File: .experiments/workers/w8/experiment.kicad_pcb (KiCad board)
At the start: 2 copper layers, 140 x 90 mm, 39 parts, among them J1 USB_C, J2 Output, J3 Debug, Q1 FS8205A, U1 USBLC6-2SC6, U2 BQ24072, U3 HY2113-KB5B, U4 MT3608, U5 AP2112K-3.3, U6 LN61CN3302MR-G

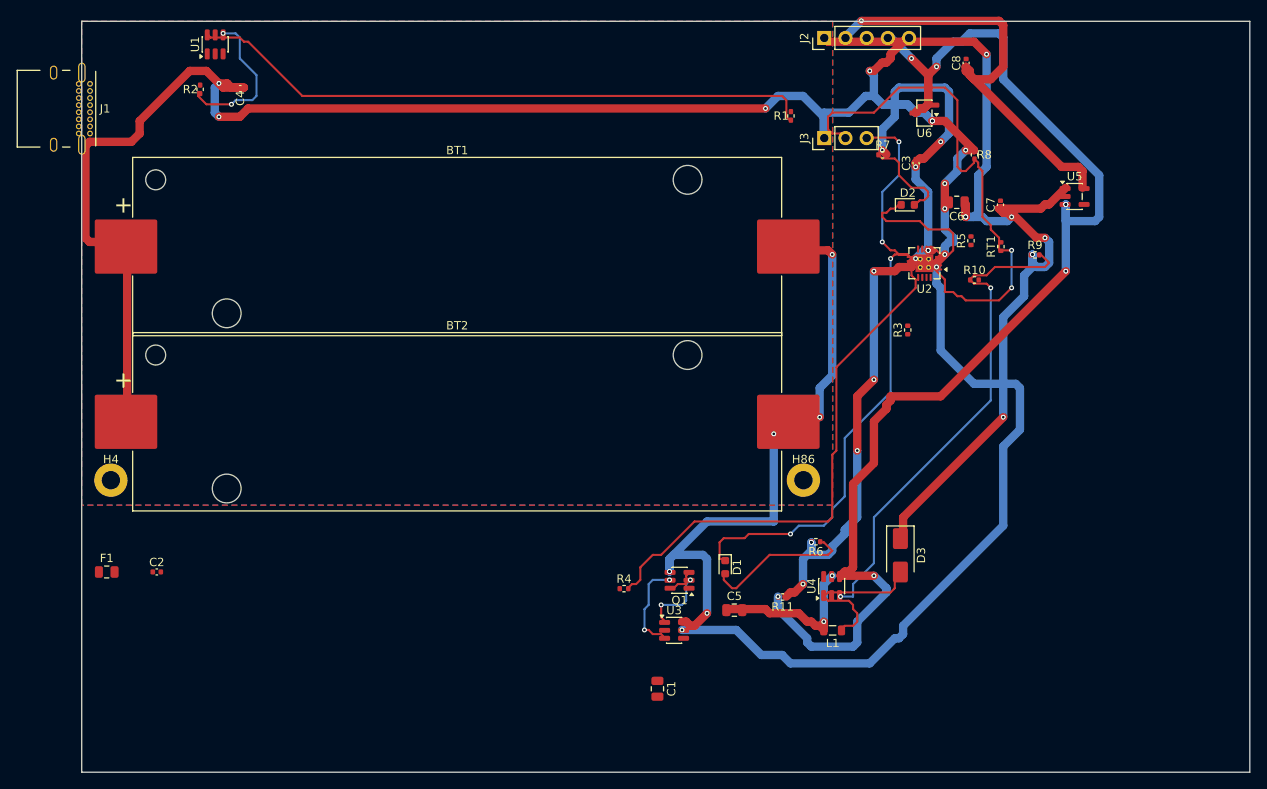
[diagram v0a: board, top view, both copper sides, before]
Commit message: 35-round experiment: best score 25.33, improved routing params
Router and conflict resolution tuning from autonomous optimization loop.
Best config: clearance=0.2051mm, cooling_factor=0.9735, existing_trace_cost=200.0

Co-Authored-By: Claude Opus 4.6 <noreply@anthropic.com>
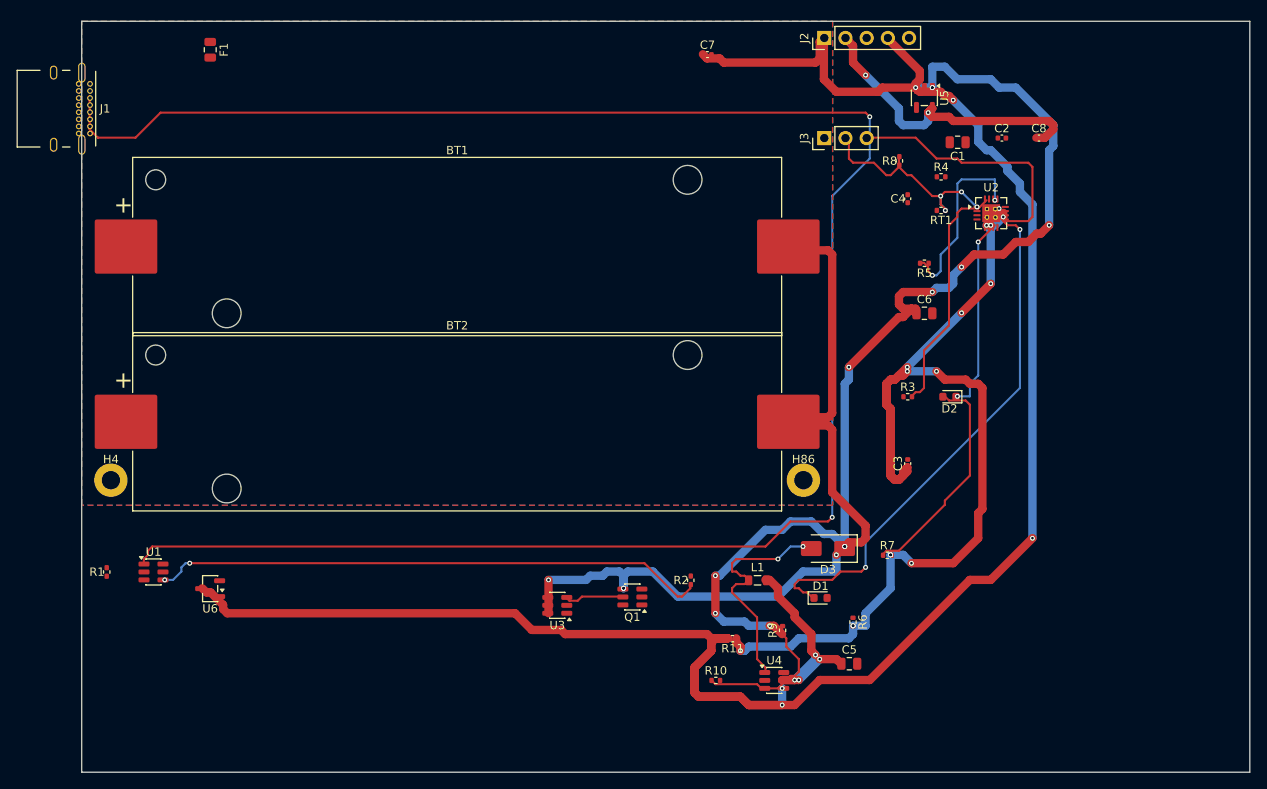
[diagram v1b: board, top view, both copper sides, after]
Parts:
- moved C2 113.9 mm to (110.3, 14.0)
- moved U6 102.8 mm to (15.4, 68.0)
- moved R1 98.5 mm to (3.00, 66.0)
- moved R2 83.2 mm to (73.0, 67.0)
- moved C4 81.1 mm to (99.0, 21.3), turned to 90 degrees
- moved C1 74.7 mm to (105.0, 14.5), turned to 180 degrees
- moved F1 63.8 mm to (15.4, 3.42), turned to -90 degrees
- moved U1 63.7 mm to (8.60, 66.0), turned to 0 degrees
- moved R4 62.3 mm to (103.0, 18.6)
- moved R10 57.1 mm to (76.0, 79.0)
- moved R9 54.2 mm to (84.0, 73.0), turned to 90 degrees
- moved R7 48.0 mm to (96.6, 64.0)
- moved C7 39.5 mm to (75.0, 4.00), turned to 0 degrees
- moved C3 36.0 mm to (99.0, 53.0)
- moved D2 23.5 mm to (104.0, 45.0), turned to 180 degrees
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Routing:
- net /VBAT: track 293.0 -> 0.00 mm, vias 14 -> 0
- net Net-(J1-CC1): track 0.00 -> 234.6 mm, vias 0 -> 2
- net Net-(R1-Pad1): track 75.5 -> 0.00 mm
- net /EN: track 149.0 -> 216.1 mm, vias 8 -> 4
- net Net-(U2-ILIM): track 62.7 -> 0.00 mm
- net Net-(R2-Pad1): track 18.4 -> 66.7 mm
- net /5V: track 115.5 -> 159.9 mm, vias 8 -> 12
- net Net-(U4-FB): track 60.0 -> 18.1 mm, vias 2 -> 0
- net /NTC_SENSE: track 62.8 -> 27.3 mm, vias 2 -> 5
- net /VSYS: track 93.0 -> 127.8 mm, vias 12 -> 14
- net Net-(U2-ISET): track 0.00 -> 28.7 mm
- net /CELL_NEG: track 75.5 -> 102.5 mm, vias 6 -> 4
- net Net-(U2-TMR): track 0.00 -> 22.2 mm, vias 0 -> 2
- net /CHG_N: track 75.4 -> 94.5 mm, vias 4 -> 2
- net Net-(D1-A): track 17.7 -> 0.00 mm
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
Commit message: 45-round experiment: best score 25.66, all nets routed (26/26)
Fixed A* performance by increasing max_search from 100k->500k to handle
high trace costs (100.0) without timing out. Kept high cost + coarse grid
(0.5mm) to prevent shorts while still routing efficiently.

Best config: edge_margin=5.7493mm, cooling_factor=0.9764, existing_trace_cost=200, max_rips=8

Co-Authored-By: Claude Opus 4.6 <noreply@anthropic.com>
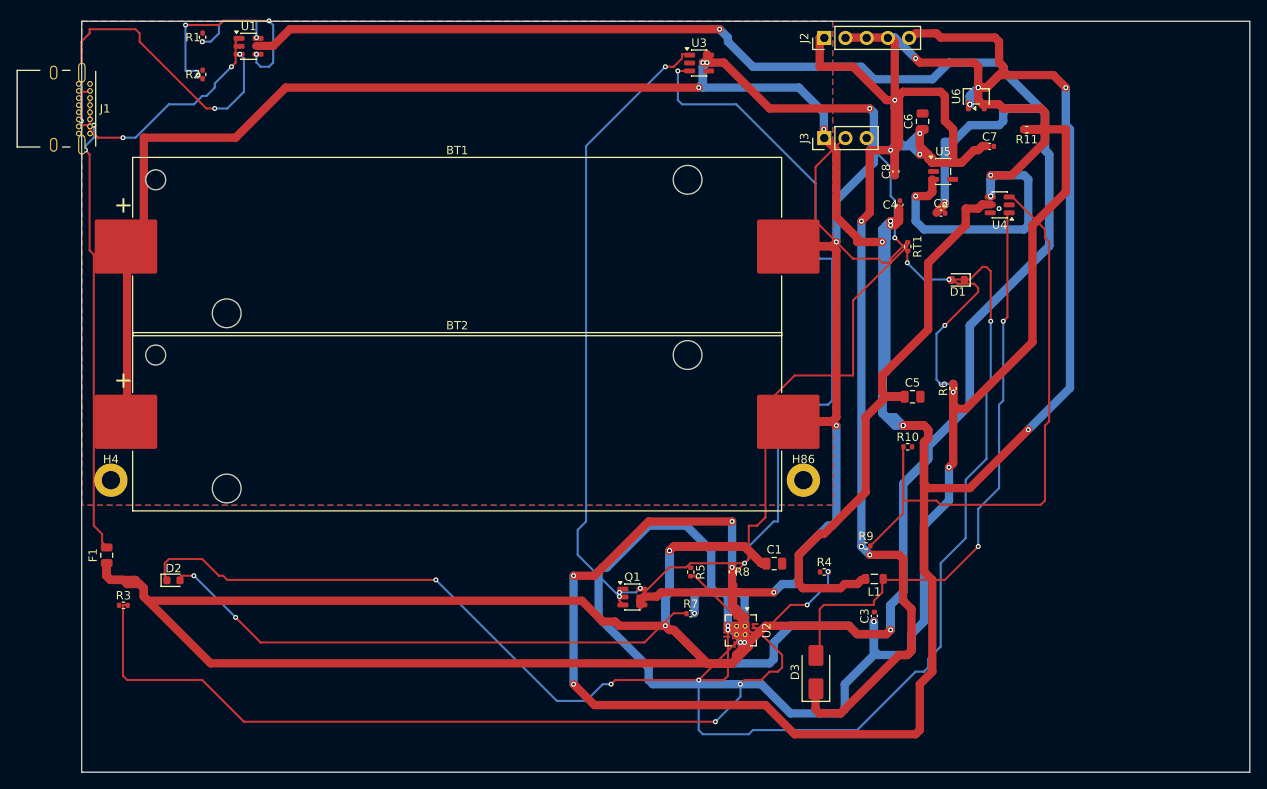
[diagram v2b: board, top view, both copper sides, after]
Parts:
- moved U6 109.1 mm to (107.2, 9.00), turned to 90 degrees
- moved R3 97.3 mm to (5.00, 70.0)
- moved D2 95.6 mm to (11.0, 67.0), turned to 0 degrees
- moved R2 84.3 mm to (14.5, 6.38)
- moved R11 70.5 mm to (113.3, 13.0)
- moved U3 67.2 mm to (74.0, 5.00), turned to 0 degrees
- moved R1 65.1 mm to (14.5, 1.92)
- moved U1 64.0 mm to (20.0, 3.00)
- moved U4 63.1 mm to (110.0, 22.0), turned to 180 degrees
- moved F1 61.8 mm to (3.00, 64.0), turned to 90 degrees
- moved U2 58.3 mm to (79.0, 73.0), turned to -90 degrees
- moved C1 55.1 mm to (83.0, 65.0), turned to 0 degrees
- moved R8 53.2 mm to (78.0, 66.0), turned to -90 degrees
- moved R4 49.4 mm to (89.0, 66.0)
- moved R5 46.4 mm to (73.0, 66.0), turned to -90 degrees
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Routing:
- net /VBUS: track 0.00 -> 543.8 mm, vias 0 -> 6
- net /VBAT: track 0.00 -> 446.4 mm, vias 0 -> 20
- net Net-(J1-CC1): track 234.6 -> 29.1 mm
- net /EN: track 216.1 -> 76.9 mm, vias 4 -> 6
- net Net-(Q1B-G): track 7.41 -> 92.2 mm, vias 0 -> 2
- net Net-(Q1A-G): track 0.00 -> 74.3 mm, vias 0 -> 2
- net Net-(U2-ISET): track 28.7 -> 100.3 mm, vias 0 -> 2
- net Net-(D2-K): track 23.2 -> 83.2 mm
- net /VSYS: track 127.8 -> 187.0 mm, vias 14 -> 8
- net Net-(U4-FB): track 18.1 -> 76.6 mm
- net Net-(F1-Pad2): track 0.00 -> 58.4 mm, vias 0 -> 2
- net /NTC_SENSE: track 27.3 -> 85.1 mm, vias 5 -> 1
- net /VSYS_BOOST: track 25.6 -> 69.8 mm, vias 4 -> 0
- net Net-(D3-A): track 27.8 -> 70.4 mm
- net Net-(J1-CC2): track 0.00 -> 40.0 mm, vias 0 -> 4
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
